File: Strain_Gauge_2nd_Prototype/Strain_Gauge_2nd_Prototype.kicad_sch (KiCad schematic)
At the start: 63 parts, among them J1 TC2030, J2 SD_Card_Receptacle, J3 Conn_01x04, J4 Conn_01x04, J5 Conn_01x04, J6 Conn_01x04, J7 Conn_01x04, J8 Conn_01x04, J9 USB4105-GF-A-060, SW1 SW_Push, U1 ADS131M08xPBS, U2 STM32F446RETx, U3 TPS73733DCQ, Y1 8.192MHz

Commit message: Adding new data, schematic with final information. Needs to be organized out properly and made to look pretty but it should work
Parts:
- removed J2: SD_Card_Receptacle, symbol Connector:SD_Card_Receptacle
- removed R7: 22-33, Resistor_SMD:R_0805_2012Metric_Pad1.20x1.40mm_HandSolder, symbol Device:R
- removed R8: 10k, Resistor_SMD:R_0805_2012Metric_Pad1.20x1.40mm_HandSolder, symbol Device:R
- added C19, C20, C24, C27, C28: 100nF, Capacitor_SMD:C_0805_2012Metric_Pad1.18x1.45mm_HandSolder, symbol Device:C
- added C21: 10uF, Capacitor_SMD:C_0805_2012Metric_Pad1.18x1.45mm_HandSolder, symbol Device:C
- added C22: 220nF, Capacitor_SMD:C_0805_2012Metric_Pad1.18x1.45mm_HandSolder, symbol Device:C
- added C23: 1uF, Capacitor_SMD:C_0805_2012Metric_Pad1.18x1.45mm_HandSolder, symbol Device:C
- added C25, C26: 22uF, Capacitor_SMD:C_0805_2012Metric_Pad1.18x1.45mm_HandSolder, symbol Device:C
- added C29: 1microF, Capacitor_SMD:C_0805_2012Metric_Pad1.18x1.45mm_HandSolder, symbol Device:C
- added D1: BZT52-C15S-AU_R1_000A1, Diode_SMD:D_SOD-323_HandSoldering, symbol Device:D_Zener
- added D2: TPSMF4L26A, Diode_SMD:D_SOD-123F, symbol Device:D_Zener
- added D3: LED, Diode_SMD:D_0805_2012Metric_Pad1.15x1.40mm_HandSolder, symbol Device:LED
- added J10: 2601-1104, CONN4_2601-1104_WAG, symbol 2026-10-21_05-43-36:2601-1104
- added J11: Molex_104031-0811, Connector_Card:microSD_HC_Molex_104031-0811, symbol Connector:Micro_SD_Card_Det2
- added L1: 8.2uH, 86m, Inductor_SMD:L_Vishay_IHLP-1616, symbol Device:L
- added Q1: PMV100EPA, Package_TO_SOT_SMD:SOT-23_Handsoldering, symbol Transistor_FET:DMP3099L
- added R29: 120, Resistor_SMD:R_0805_2012Metric_Pad1.20x1.40mm_HandSolder, symbol Device:R
- added R30: 10k, Resistor_SMD:R_0805_2012Metric_Pad1.20x1.40mm_HandSolder, symbol Device:R
- added R31: 10K, Resistor_SMD:R_0805_2012Metric_Pad1.20x1.40mm_HandSolder, symbol Device:R_US
- added R32, R33: 100k, Resistor_SMD:R_0805_2012Metric_Pad1.20x1.40mm_HandSolder, symbol Device:R_US
- added R34: 24.9k, Resistor_SMD:R_0805_2012Metric_Pad1.20x1.40mm_HandSolder, symbol Device:R_US
- added R35: 500, Resistor_SMD:R_0805_2012Metric_Pad1.20x1.40mm_HandSolder, symbol Device:R_US
- added R36: 2.2k, Resistor_SMD:R_0805_2012Metric_Pad1.20x1.40mm_HandSolder, symbol Device:R_US
- added R37: 33, Resistor_SMD:R_0805_2012Metric_Pad1.20x1.40mm_HandSolder, symbol Device:R
- added U4: MCP2562-E-SN, Package_SO:SOIC-8_3.9x4.9mm_P1.27mm, symbol Interface_CAN_LIN:MCP2562-E-SN
- added U5: LMR33610ADDAR, Package_SO:Texas_HSOP-8-1EP_3.9x4.9mm_P1.27mm_ThermalVias, symbol Regulator_Switching:LMR33610ADDAR
- added U6: TPS2113APWR, TPS2113APWR:SOP65P640X120-8N, symbol TPS2113APWR:TPS2113APWR
- C16: value 10uF -> 4.7microF
- C9: value 10-100nF (Choose from Oscillator Datasheet) -> 100nF
- TP1: footprint Connector:Banana_Jack_1Pin -> TestPoint:TestPoint_Pad_D1.5mm
- Y1: value 8.192MHz -> 7XL-8.192MBD-T
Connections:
- net 3.3V: now also C20.1, J11.4 (VDD), R36.1, U4.5 (Vio)
- net CARDDETECT: now also J11.10 (DET_A)
- net CMD: now also J11.3 (CMD)
- net DAT0: now also J11.7 (DAT0)
- net DAT1: now also J11.8 (DAT1)
- net DAT2: now also J11.1 (DAT2)
- net DAT3: now also J11.2 (DAT3/CD)
- net GND: now also C19.1, C20.2, C21.2, C22.2, C23.2, C25.2, C26.2, C27.2, C28.2, C29.2, D2.2 (A), J10.5 (3_1), J10.6 (3_2), J11.6 (VSS), J11.9 (DET_B), J11.SH (SHIELD), R30.2, R31.2, R34.2, R35.1, U4.2 (VSS), U5.1 (GND), U5.9 (GND), U6.2 (~{EN}), U6.5 (GND)
- net SDCLK: now also R37.1
- net USB_5V_Fused: now also C27.1, U6.6 (IN2); no longer U3.1 (IN), U3.5 (EN)
- net CAN_STBY: now reaches U2.58 (PB6)
- net CAN_STBY: now also R30.1, U4.8 (STBY)
- net CAN_RX: now reaches U2.61 (PB8)
- net CAN_RX: now also U4.4 (RXD)
- net CAN_TX: now reaches U2.62 (PB9)
- net CAN_TX: now also U4.1 (TXD)
- net WRITEPROTECT: no longer names the net of U2.29 (PB10)
- new net: J11.5 (CLK), R37.2
- new net: D3.2 (A), R36.2
- new net: D3.1 (K), U6.1 (STAT)
- new net: D1.2 (A), Q1.1 (G), R31.1
- new net: C24.1, U5.7 (BOOT)
- new net 5V: C19.2, C29.1, U3.1 (IN), U3.5 (EN), U4.3 (VDD), U6.7 (OUT)
- new net BUCK_OUT: C25.1, C26.1, C28.1, L1.2, R33.1, U6.3 (VSNS), U6.8 (IN1)
- new net Bat_POS: D2.1 (K), J10.7 (4_1), J10.8 (4_2), Q1.3 (D)
- new net CANH: J10.1 (1_1), J10.2 (1_2), R29.1, U4.7 (CANH)
- new net CANL: J10.3 (2_1), J10.4 (2_2), R29.2, U4.6 (CANL)
- new net FB: R33.2, R34.1, U5.5 (FB)
- new net ILIM: R35.2, U6.4 (ILIM)
- new net PG: R32.1, U5.4 (PG)
- new net SW: C24.2, L1.1, U5.8 (SW)
- new net buckIN: C21.1, C22.1, D1.1 (K), Q1.2 (S), U5.2 (VIN), U5.3 (EN)
- new net buckVCC: C23.1, R32.2, U5.6 (VCC)
- no-connect marks 37 -> 35
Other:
- note added: "4wire debugger"
- note added: "CAN Transciever"
- note added: "DO NOT PLACE UNLESS END OF BUS"
- note added: "Reverse Polarity Protection and TVS"
- note added: "SMPS"
- note removed: "Be sure to match the oscillator layout with the one that is bought"
- moved on the sheet: C15, C16, C18, C4, C9, F1, J3, J4, J5, J6, J7, J8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

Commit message: The netlist has been updated for the schematic for review
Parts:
- added J2: Conn_01x04, symbol Connector_Generic:Conn_01x04
- J3, J4, J5: footprint Connector_Wire:SolderWire-0.25sqmm_1x04_P4.5mm_D0.65mm_OD2mm_Relief2x -> Connector_Wire:SolderWire-0.25sqmm_1x04_P4.5mm_D0.65mm_OD2mm
- J6, J7, J8: footprint Connector_Wire:SolderWire-0.25sqmm_1x04_P4.5mm_D0.65mm_OD2mm_Relief2x -> SolderWire-0.25sqmm_1x04_P4.5mm_D0.65mm_OD2mm
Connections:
- net 3.3V: now also J2.1 (Pin_1)
- net GND: now also J2.3 (Pin_3)
- net NRST: now also J2.2 (Pin_2)
- net SWO: now also J2.4 (Pin_4)
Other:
- note added: "CAN Transciever and operators"
- note added: "External Connectors"
- note added: "GAUGE Connections"
- note added: "Look into possibility of an RF protection device for the ADS?"
- note added: "Make Sure to get shielded Inductor"
- note added: "Power modulators and control units"
- note added: "SD Card writing"
- note added: "USB Input"
- moved on the sheet: C27, C28, C29, D3, J1, J10, R35, R36, U6

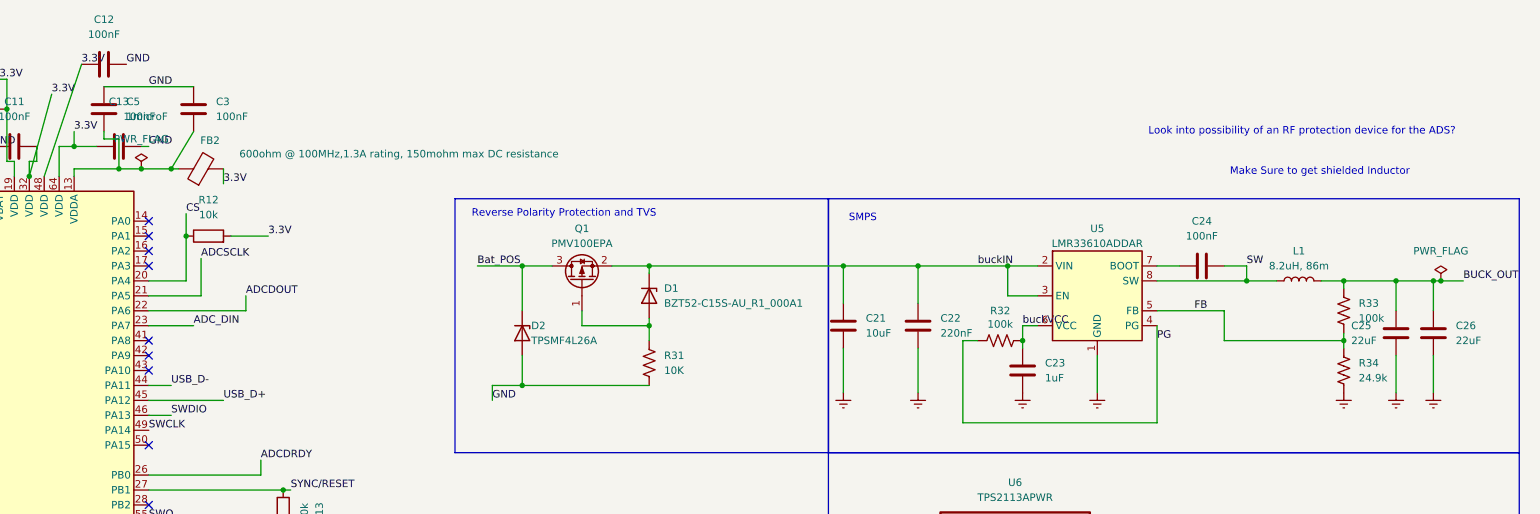
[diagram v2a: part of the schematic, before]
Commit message: PCB components are laid out, need to position, then route.
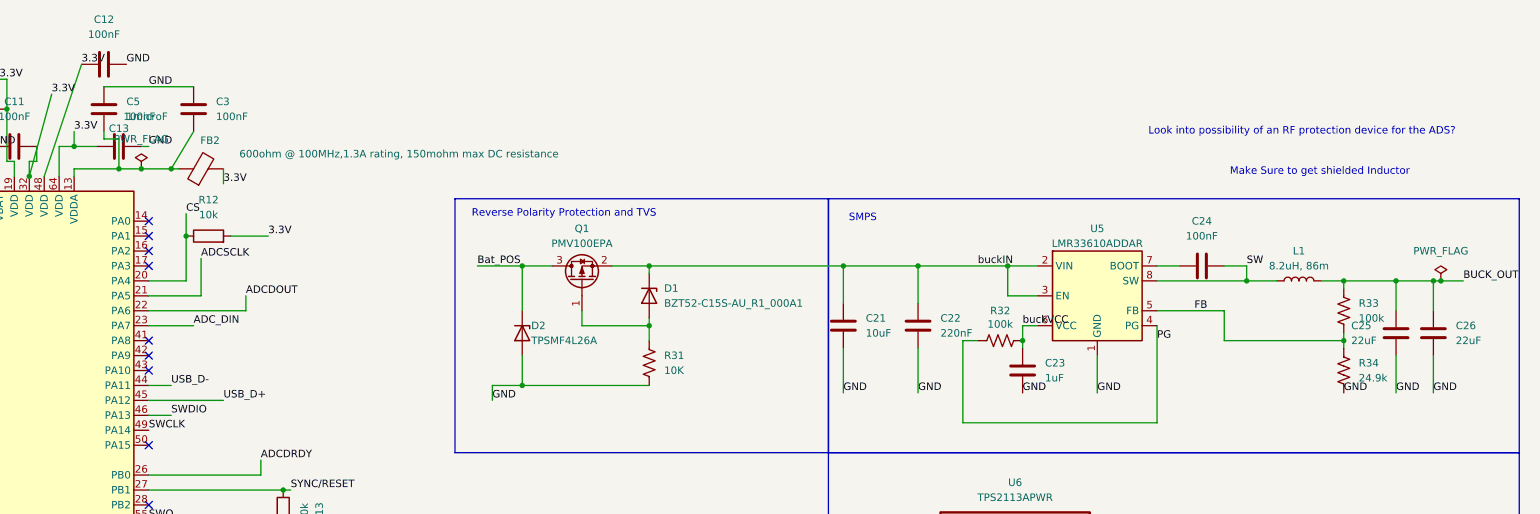
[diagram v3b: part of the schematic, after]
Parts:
- J2: footprint (none) -> Connector_Wire:SolderWire-0.25sqmm_1x04_P4.5mm_D0.65mm_OD2mm
- J9: footprint USB4105-GF-A-060:GCT_USB4105-GF-A-060 -> Gauge Footprints:GCT_USB4105-GF-A-060
- U3: footprint TPS73733DCQ:SOT127P706X180-6N -> Gauge Footprints:SOT127P706X180-6N
- U6: footprint TPS2113APWR:SOP65P640X120-8N -> Gauge Footprints:SOP65P640X120-8N

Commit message: This is the update with STM32CUBEMX and IDE, to check syntax
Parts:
- added U7: ADS131E08IPAG, PAG0064A_N, symbol 2026-10-22_23-36-45:ADS131E08IPAG
- added U8: STM32F412RET6, Gauge Footprints:LQFP64-10x10mm, symbol 2026-10-23_00-01-03:STM32F412RET6
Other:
- moved on the sheet: C9, R30, Y1

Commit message: Redoing schematic now, have done parts of it already, just need to redo ADS and then footprints then should be okay to route
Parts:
- removed U8: STM32F412RET6, Gauge Footprints:LQFP64-10x10mm, symbol 2026-10-23_00-01-03:STM32F412RET6
- added C30: 1microF, Capacitor_SMD:C_1206_3216Metric_Pad1.33x1.80mm_HandSolder, symbol Device:C
- added C31: 100nF - VDDUSB, Capacitor_SMD:C_0402_1005Metric_Pad0.74x0.62mm_HandSolder, symbol Device:C
- added C32: 4.7microF - General all board one, Capacitor_SMD:C_0603_1608Metric_Pad1.08x0.95mm_HandSolder, symbol Device:C
- added C33: 100nF, Capacitor_SMD:C_0402_1005Metric_Pad0.74x0.62mm_HandSolder, symbol Device:C
- added R38, R39, R40, R41, R42, R43, R44, R45, R46: 10K, Resistor_SMD:R_0402_1005Metric_Pad0.72x0.64mm_HandSolder, symbol Device:R_US
- added SW2: SW_Push, Button_Switch_THT:SW_PUSH_6mm, symbol Switch:SW_Push
- added TP2: TestPoint, TestPoint:TestPoint_Pad_D1.5mm, symbol Connector:TestPoint
- added U8: STM32L476RGTx, Package_QFP:LQFP-64_10x10mm_P0.5mm, symbol MCU_ST_STM32L4:STM32L476RGTx
- C10, C11, C12, C13, C15, C19, C20, C22, C24, C3, C7, C8, C9: footprint Capacitor_SMD:C_0805_2012Metric_Pad1.18x1.45mm_HandSolder -> Capacitor_SMD:C_0402_1005Metric_Pad0.74x0.62mm_HandSolder
- C16: footprint Capacitor_SMD:C_1206_3216Metric_Pad1.33x1.80mm_HandSolder -> Capacitor_SMD:C_0603_1608Metric_Pad1.08x0.95mm_HandSolder
- C18: footprint Capacitor_SMD:C_1206_3216Metric_Pad1.33x1.80mm_HandSolder -> Capacitor_SMD:C_0402_1005Metric_Pad0.74x0.62mm_HandSolder
- C23, C25, C26, C4, C6: footprint Capacitor_SMD:C_0805_2012Metric_Pad1.18x1.45mm_HandSolder -> Capacitor_SMD:C_1206_3216Metric_Pad1.33x1.80mm_HandSolder
- R10, R26, R27, R28, R31, R34, R36, R37: footprint Resistor_SMD:R_0805_2012Metric_Pad1.20x1.40mm_HandSolder -> Resistor_SMD:R_0402_1005Metric_Pad0.72x0.64mm_HandSolder
- R29, R33: footprint Resistor_SMD:R_0805_2012Metric_Pad1.20x1.40mm_HandSolder -> Resistor_SMD:R_0402_1005Metric
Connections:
- net 3.3V: now also C13.2, C3.1, C31.1, C32.1, R38.2, R39.2, R40.2, R41.2, R42.2, R43.2, R45.2, U8.1 (VBAT), U8.19 (VDD), U8.32 (VDD), U8.48 (VDDUSB), U8.64 (VDD); no longer C12.1, C13.1, U2.48 (VDD), U2.64 (VDD)
- net ADCDOUT: now also U8.22 (PA6)
- net ADCDRDY: now also U8.26 (PB0)
- net ADCSCLK: now also U8.21 (PA5)
- net CAN_RX: now also U8.61 (PB8)
- net CAN_STBY: now also R46.1, U8.59 (PB7)
- net CAN_TX: now also U8.62 (PB9)
- net CARDDETECT: now also R43.1, U8.57 (PB5)
- net GND: now also C13.1, C3.2, C30.1, C31.2, C32.2, C33.2, R44.2, R46.2, SW2.1, U8.12 (VSSA), U8.18 (VSS), U8.31 (VSS), U8.47 (VSS), U8.63 (VSS); no longer C13.2, C3.1, C5.1
- net NRST: now also C33.1, SW2.2, U8.7 (NRST)
- net SWCLK: now also U8.49 (PA14)
- net SWDIO: now also U8.46 (PA13)
- net SWO: now also U8.55 (PB3)
- net USB_D+: now also U8.45 (PA12)
- net USB_D-: now also U8.44 (PA11)
- new net: C12.1, C30.2, FB2.1, U8.13 (VDDA)
- new net: R44.1, TP2.1, U8.60 (BOOT0)
- new net ADCCS: R45.1, U8.20 (PA4)
- new net ADCDIN: U8.23 (PA7)
- new net ADCSTART: U8.27 (PB1)
- new net OSCIN: U8.3 (PC14)
- new net OSCOUT: U8.4 (PC15)
- new net SDMMC_CK: U8.53 (PC12)
- new net SDMMC_CMD: R42.1, U8.2 (PC13)
- new net SDMMC_D0: R38.1, U8.39 (PC8)
- new net SDMMC_D1: R39.1, U8.40 (PC9)
- new net SDMMC_D2: R40.1, U8.51 (PC10)
- new net SDMMC_D3: R41.1, U8.52 (PC11)
- now unconnected: C5.2, U2.13 (VDDA)
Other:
- note added: "Frequency: 32.768 kHz Type: tuning-fork crystal Load capacitance: preferably 6–9 pF ESR: within STM32L476 LSE limits Package: suitable for hand assembly"
- moved on the sheet: C1, C10, C11, C13, C14, C17, C2, C3, C5, R1, R11, R12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

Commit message: Have redone the design, should be close to be routing. May just need to change the size of the 1uF capacitors down to get them closer to the ADS?
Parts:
- removed C1, C14: 4.7microF, Capacitor_SMD:C_0805_2012Metric_Pad1.18x1.45mm_HandSolder, symbol Device:C
- removed C17, C2: 100nF, Capacitor_SMD:C_0805_2012Metric_Pad1.18x1.45mm_HandSolder, symbol Device:C
- removed C4, C6: 1microF, Capacitor_SMD:C_1206_3216Metric_Pad1.33x1.80mm_HandSolder, symbol Device:C
- removed C5: 1microF, Capacitor_SMD:C_0805_2012Metric_Pad1.18x1.45mm_HandSolder, symbol Device:C
- removed C7, C9: 100nF, Capacitor_SMD:C_0402_1005Metric_Pad0.74x0.62mm_HandSolder, symbol Device:C
- removed C8: 220nF, Capacitor_SMD:C_0402_1005Metric_Pad0.74x0.62mm_HandSolder, symbol Device:C
- removed L1: 8.2uH, 86m, Inductor_SMD:L_Vishay_IHLP-1616, symbol Device:L
- removed R1, R11, R12, R13, R2, R3, R30, R4, R5, R6: 10k, Resistor_SMD:R_0805_2012Metric_Pad1.20x1.40mm_HandSolder, symbol Device:R
- removed R10: 33, Resistor_SMD:R_0402_1005Metric_Pad0.72x0.64mm_HandSolder, symbol Device:R
- removed R9: 33, Resistor_SMD:R_0805_2012Metric_Pad1.20x1.40mm_HandSolder, symbol Device:R
- removed SW1: SW_Push, Button_Switch_THT:SW_PUSH_6mm, symbol Switch:SW_Push
- removed TP1: TestPoint, TestPoint:TestPoint_Pad_D1.5mm, symbol Connector:TestPoint
- removed U1: ADS131M08xPBS, Package_QFP:TQFP-32_5x5mm_P0.5mm, symbol Analog_ADC:ADS131M08xPBS
- removed U2: STM32F446RETx, Package_QFP:LQFP-64_10x10mm_P0.5mm, symbol MCU_ST_STM32F4:STM32F446RETx
- removed Y1: 7XL-8.192MBD-T, Oscillator:Oscillator_SMD_Abracon_ASE-4Pin_3.2x2.5mm, symbol Oscillator:ASE-xxxMHz
- added C34, C35, C36, C37, C38, C39, C46, C47, C50, C53: 100nF, Capacitor_SMD:C_0402_1005Metric_Pad0.74x0.62mm_HandSolder, symbol Device:C
- added C40, C41, C42, C43, C44, C45, C48, C49, C52, C54, C55: 1microF, Capacitor_SMD:C_1206_3216Metric_Pad1.33x1.80mm_HandSolder, symbol Device:C
- added C51: 10uF, Capacitor_SMD:C_0805_2012Metric_Pad1.18x1.45mm_HandSolder, symbol Device:C
- added C56: 22uF, Capacitor_SMD:C_1206_3216Metric_Pad1.33x1.80mm_HandSolder, symbol Device:C
- added C57, C58: 10pF, Capacitor_SMD:C_0603_1608Metric_Pad1.08x0.95mm_HandSolder, symbol Device:C
- added FB3: 600ohm @ 100MHz,1.3A rating, 150mohm max DC resis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, Inductor_SMD:L_0603_1608Metric_Pad1.05x0.95mm_HandSolder, symbol Device:FerriteBead
- added L2: IHLP2525CZER8R2M01, Gauge Footprints:INDPM6965X300N, symbol IHLP2525CZER8R2M01:IHLP2525CZER8R2M01
- added R47, R48, R51, R52, R53, R54: 10K, Resistor_SMD:R_0402_1005Metric_Pad0.72x0.64mm_HandSolder, symbol Device:R_US
- added Y1: ECS-.327-9-34B-TR, Gauge Footprints:XTAL_ECS-.327-9-34B-TR, symbol ECS-.327-9-34B-TR:ECS-.327-9-34B-TR
- D3: footprint Diode_SMD:D_0805_2012Metric_Pad1.15x1.40mm_HandSolder -> LED_SMD:LED_0402_1005Metric
- J6, J7, J8: footprint SolderWire-0.25sqmm_1x04_P4.5mm_D0.65mm_OD2mm -> Connector_Wire:SolderWire-0.25sqmm_1x04_P4.5mm_D0.65mm_OD2mm
- R14, R15, R16, R17, R18, R19, R20, R21, R22, R23, R24, R25: footprint Resistor_SMD:R_0805_2012Metric_Pad1.20x1.40mm_HandSolder -> Resistor_THT:R_Axial_DIN0207_L6.3mm_D2.5mm_P10.16mm_Horizontal
- U7: footprint PAG0064A_N -> Gauge Footprints:PAG0064A_L
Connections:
- net CMD is gone; now on net SDMMC_CMD: J11.3 (CMD)
- net DAT0 is gone; now on net SDMMC_D0: J11.7 (DAT0)
- net DAT1 is gone; now on net SDMMC_D1: J11.8 (DAT1)
- net DAT2 is gone; now on net SDMMC_D2: J11.1 (DAT2)
- net DAT3 is gone; now on net SDMMC_D3: J11.2 (DAT3/CD)
- net SDCLK is gone; now on net SDMMC_CK: R37.1
- net 3.3V: now also U7.48 (DVDD), U7.50 (DVDD), U7.52 (CLKSEL), C46.2, C47.2, C48.1, C49.1, FB3.2, R47.2, R48.2; no longer J3.1 (Pin_1), J4.1 (Pin_1), J5.1 (Pin_1), J6.1 (Pin_1), J7.1 (Pin_1), J8.1 (Pin_1), R14.1, R16.1, R18.1, R20.1, R22.1, R24.1
- net ADCCS: now also U7.39 (CS_N)
- net ADCDIN: now also U7.34 (DIN)
- net ADCDOUT: now also U7.43 (DOUT)
- net ADCDRDY: now also U7.47 (DRDY_N)
- net ADCSCLK: now also U7.40 (SCLK)
- net ADCSTART: now also U7.38 (START)
- net BUCK_OUT: now also L2.2
- net CARDDETECT: now also U8.2 (PC13); no longer U8.57 (PB5)
- net GND: now also U7.20 (AVSS), U7.23 (AVSS), U7.25 (VREFN), U7.31 (RESV1), U7.32 (AVSS), U7.33 (DGND), U7.37 (CLK), U7.41 (DAISY_IN), U7.49 (DGND), U7.51 (DGND), U7.53 (AVSS1), U7.57 (AVSS), U7.58 (AVSS), U7.60 (OPAMPP), C34.1, C35.1, C36.1, C37.1, C38.1, C39.1, C40.2, C41.2, C42.2, C43.2, C44.2, C45.2, C46.1, C47.1, C48.2, C49.2, C50.1, C51.2, C52.2, C53.1, C54.1, C55.2, C56.2, C57.2, C58.2, R51.2, R52.2, R53.2, R54.2
- net OSCIN: now also C57.1, Y1.1
- net OSCOUT: now also C58.1, Y1.2
- net SDMMC_CMD: now also U8.54 (PD2); no longer U8.2 (PC13)
- net SW: now also L2.1
- net V0+: now also U7.16 (IN1P)
- net V0-: now also U7.15 (IN1N)
- net V1+: now also U7.14 (IN2P)
- net V1-: now also U7.13 (IN2N)
- net V2+: now also U7.12 (IN3P)
- net V2-: now also U7.11 (IN3N)
- net V3+: now also U7.10 (IN4P)
- net V3-: now also U7.9 (IN4N)
- net V4+: now also U7.8 (IN5P)
- net V4-: now also U7.7 (IN5N)
- net V5+: now also U7.6 (IN6P)
- net V5-: now also U7.5 (IN6N)
- net 3.3VAnalog: now reaches U7.1 (IN8N)
- net 3.3VAnalog: now also J3.1 (Pin_1), J4.1 (Pin_1), J5.1 (Pin_1), J6.1 (Pin_1), J7.1 (Pin_1), J8.1 (Pin_1), R14.1, R16.1, R18.1, R20.1, R22.1, R24.1, U7.19 (AVDD), U7.2 (IN8P), U7.21 (AVDD), U7.22 (AVDD), U7.24 (VREFP), U7.3 (IN7N), U7.4 (IN7P), U7.54 (AVDD1), U7.56 (AVDD), U7.59 (AVDD), C34.2, C35.2, C36.2, C37.2, C38.2, C39.2, C40.1, C41.1, C42.1, C43.1, C44.1, C45.1, C50.2, C51.1, FB3.1
- net at U7.26 (VCAP4): now also C55.1
- net at U7.28 (VCAP1): now also C56.1
- net at U7.30 (VCAP2): now also C54.2
- net ADCPDWN: now reaches U7.35 (PWDN_N)
- net ADCPDWN: now also U8.24 (PC4), R48.1
- net ADCRESET: now reaches U7.36 (RESET_N)
- net ADCRESET: now also U8.25 (PC5), R47.1
- net at U7.42 (GPIO1): now also R51.1
- net at U7.44 (GPIO2): now also R52.1
- net at U7.45 (GPIO3): now also R53.1
- net at U7.46 (GPIO4): now also R54.1
- net at U7.55 (VCAP3): now also C52.1, C53.2
- no-connect marks 35 -> 36
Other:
- moved on the sheet: C20, J6, R20, R21, R43, U7
